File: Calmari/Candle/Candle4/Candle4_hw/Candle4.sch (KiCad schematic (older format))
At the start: 59 parts, among them Q1 LED_RGB, SW1 BUTTON, SW2 BUTTON, SW3 BUTTON

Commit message: 
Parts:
- removed RP1, RP2, RP3: REFPOINT, symbol REFPOINT
- R1: value 20k -> 30k
- R7, R8: value 10R -> 51R
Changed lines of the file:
@@
 EESchema Schematic File Version 2
-LIBS:Connectors_kl
-LIBS:pcb_details
-LIBS:RF ICs
-LIBS:st_kl
-LIBS:Tittar_kl
-LIBS:power
-LIBS:Antennas_kl
-LIBS:Power_kl
 LIBS:Candle4-cache
 EELAYER 27 0
@@
 NoConn ~ 5250 3000
 NoConn ~ 5250 2700
-NoConn ~ 5250 2600
 NoConn ~ 5250 2500
 NoConn ~ 5250 2400
@@
 P 12100 7150
 F 0 "R7" V 12180 7000 50  0000 C CNN
-F 1 "10R" V 12100 7150 50  0000 C CNN
+F 1 "51R" V 12100 7150 50  0000 C CNN
 F 2 "RES_0603" V 12180 7250 28  0000 C CNN
 F 3 "~" H 12100 7150 60  0000 C CNN
@@
 P 12100 7350
 F 0 "R8" V 12180 7200 50  0000 C CNN
-F 1 "10R" V 12100 7350 50  0000 C CNN
+F 1 "51R" V 12100 7350 50  0000 C CNN
 F 2 "RES_0603" V 12180 7450 28  0000 C CNN
 F 3 "~" H 12100 7350 60  0000 C CNN
@@
 $EndComp
 $Comp
-L REFPOINT RP1
-U 1 1 4DC45333
-P 15350 9550
-F 0 "RP1" H 15050 9550 60  0000 C CNN
-F 1 "REFPOINT" H 14700 9550 60  0000 C CNN
-F 2 "" H 15350 9550 60  0001 C CNN
-F 3 "" H 15350 9550 60  0001 C CNN
-	1    15350 9550
-	1    0    0    -1
-$EndComp
-$Comp
-L REFPOINT RP2
-U 1 1 4DC4533D
-P 15350 9800
-F 0 "RP2" H 15050 9800 60  0000 C CNN
-F 1 "REFPOINT" H 14700 9800 60  0000 C CNN
-F 2 "" H 15350 9800 60  0001 C CNN
-F 3 "" H 15350 9800 60  0001 C CNN
-	1    15350 9800
-	1    0    0    -1
-$EndComp
-$Comp
-L REFPOINT RP3
-U 1 1 51E196D1
-P 15350 10050
-F 0 "RP3" H 15050 10050 60  0000 C CNN
-F 1 "REFPOINT" H 14700 10050 60  0000 C CNN
-F 2 "" H 15350 10050 60  0001 C CNN
-F 3 "" H 15350 10050 60  0001 C CNN
-	1    15350 10050
-	1    0    0    -1
-$EndComp
-$Comp
 L CRYSTAL_H XTAL1
 U 1 1 51E1A3DF
@@
 	1    0    0    -1
 $EndComp
-Text Label 7900 3000 0    60   ~ 0
+Text Label 4850 2200 0    60   ~ 0
 LED_R
-Text Label 7900 3200 0    60   ~ 0
+Text Label 4850 2300 0    60   ~ 0
 LED_G
-Text Label 7900 3300 0    60   ~ 0
+Text Label 4850 2600 0    60   ~ 0
 LED_B
-NoConn ~ 5250 2300
 NoConn ~ 5250 3500
 NoConn ~ 5250 3600
@@
 P 1500 7900
 F 0 "R1" V 1580 7750 50  0000 C CNN
-F 1 "20k" V 1500 7900 50  0000 C CNN
+F 1 "30k" V 1500 7900 50  0000 C CNN
 F 2 "RES_0603" V 1580 8000 28  0000 C CNN
 F 3 "~" H 1500 7900 60  0000 C CNN
@@
 Wire Wire Line
 	1650 5800 1500 5800
-Connection ~ 1500 5800
 Wire Wire Line
 	1500 6400 1650 6400
@@
 	9750 4550 9850 4550
 Wire Wire Line
-	7900 3000 7750 3000
-Wire Wire Line
-	7750 3200 7900 3200
-Wire Wire Line
-	7900 3300 7750 3300
-Wire Wire Line
 	5250 3900 5100 3900
 Wire Wire Line
@@
 Wire Wire Line
 	1500 5800 1500 7650
-NoConn ~ 5250 2200
 Text Notes 4550 8300 0    60   ~ 0
 +BATTERY
 Text Notes 4550 8800 0    60   ~ 0
 -BATTERY
+NoConn ~ 7750 3000
+NoConn ~ 7750 3200
+NoConn ~ 7750 3300
+Wire Wire Line
+	4850 2200 5250 2200
+Wire Wire Line
+	5250 2300 4850 2300
+Wire Wire Line
+	4850 2600 5250 2600
 $EndSCHEMATC

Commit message: Candle4 pcb added
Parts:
- C6, C7, C8, C9: footprint CAP_0603 -> CAP_0402
- R1, R2, R3, R4, R6, R7, R8: footprint RES_0603 -> RES_0402
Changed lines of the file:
@@
 EESchema Schematic File Version 2
+LIBS:Connectors_kl
+LIBS:pcb_details
+LIBS:RF ICs
+LIBS:st_kl
+LIBS:Tittar_kl
+LIBS:power
+LIBS:Antennas_kl
+LIBS:Power_kl
 LIBS:Candle4-cache
 EELAYER 27 0
@@
 Sheet 1 1
 Title ""
-Date "22 feb 2015"
+Date "3 mar 2015"
 Rev ""
 Comp ""
@@
 F 0 "R7" V 12180 7000 50  0000 C CNN
 F 1 "51R" V 12100 7150 50  0000 C CNN
-F 2 "RES_0603" V 12180 7250 28  0000 C CNN
+F 2 "RES_0402" V 12180 7250 28  0000 C CNN
 F 3 "~" H 12100 7150 60  0000 C CNN
 	1    12100 7150
@@
 F 0 "R8" V 12180 7200 50  0000 C CNN
 F 1 "51R" V 12100 7350 50  0000 C CNN
-F 2 "RES_0603" V 12180 7450 28  0000 C CNN
+F 2 "RES_0402" V 12180 7450 28  0000 C CNN
 F 3 "~" H 12100 7350 60  0000 C CNN
 	1    12100 7350
@@
 F 0 "R6" V 12180 6800 50  0000 C CNN
 F 1 "51R" V 12100 6950 50  0000 C CNN
-F 2 "RES_0603" V 12180 7050 28  0000 C CNN
+F 2 "RES_0402" V 12180 7050 28  0000 C CNN
 F 3 "~" H 12100 6950 60  0000 C CNN
 	1    12100 6950
@@
 F 0 "C7" H 6450 8450 50  0000 L CNN
 F 1 "10u" H 6600 8650 50  0000 L CNN
-F 2 "CAP_0603" V 6650 8400 28  0000 C BNN
+F 2 "CAP_0402" V 6650 8400 28  0000 C BNN
 F 3 "~" H 6550 8550 60  0000 C CNN
 	1    6550 8550
@@
 F 0 "C6" H 6050 8450 50  0000 L CNN
 F 1 "0.1u" H 5950 8650 50  0000 L CNN
-F 2 "CAP_0603" V 6250 8400 28  0000 C BNN
+F 2 "CAP_0402" V 6250 8400 28  0000 C BNN
 F 3 "~" H 6150 8550 60  0000 C CNN
 	1    6150 8550
@@
 F 0 "C8" H 8700 8450 50  0000 L CNN
 F 1 "0.1u" H 8600 8650 50  0000 L CNN
-F 2 "CAP_0603" V 8900 8400 28  0000 C BNN
+F 2 "CAP_0402" V 8900 8400 28  0000 C BNN
 F 3 "~" H 8800 8550 60  0000 C CNN
 	1    8800 8550
@@
 F 0 "C9" H 9100 8450 50  0000 L CNN
 F 1 "10u" H 9250 8650 50  0000 L CNN
-F 2 "CAP_0603" V 9300 8400 28  0000 C BNN
+F 2 "CAP_0402" V 9300 8400 28  0000 C BNN
 F 3 "~" H 9200 8550 60  0000 C CNN
 	1    9200 8550
@@
 F 0 "R1" V 1580 7750 50  0000 C CNN
 F 1 "30k" V 1500 7900 50  0000 C CNN
-F 2 "RES_0603" V 1580 8000 28  0000 C CNN
+F 2 "RES_0402" V 1580 8000 28  0000 C CNN
 F 3 "~" H 1500 7900 60  0000 C CNN
 	1    1500 7900
@@
 F 0 "R2" V 2980 5650 50  0000 C CNN
 F 1 "4k7" V 2900 5800 50  0000 C CNN
-F 2 "RES_0603" V 2980 5900 28  0000 C CNN
+F 2 "RES_0402" V 2980 5900 28  0000 C CNN
 F 3 "~" H 2900 5800 60  0000 C CNN
 	1    2900 5800
@@
 F 0 "R3" V 2980 6250 50  0000 C CNN
 F 1 "4k7" V 2900 6400 50  0000 C CNN
-F 2 "RES_0603" V 2980 6500 28  0000 C CNN
+F 2 "RES_0402" V 2980 6500 28  0000 C CNN
 F 3 "~" H 2900 6400 60  0000 C CNN
 	1    2900 6400
@@
 F 0 "R4" V 2980 6850 50  0000 C CNN
 F 1 "4k7" V 2900 7000 50  0000 C CNN
-F 2 "RES_0603" V 2980 7100 28  0000 C CNN
+F 2 "RES_0402" V 2980 7100 28  0000 C CNN
 F 3 "~" H 2900 7000 60  0000 C CNN
 	1    2900 7000

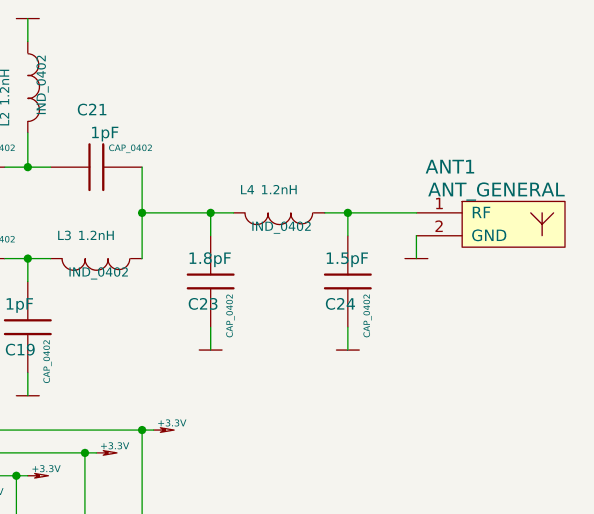
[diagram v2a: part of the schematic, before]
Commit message: 
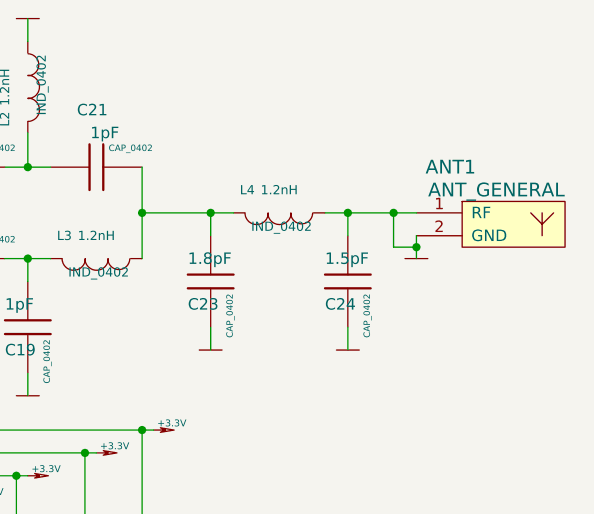
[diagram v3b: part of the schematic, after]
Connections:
- wire segments 172 -> 174
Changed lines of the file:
@@
 Sheet 1 1
 Title ""
-Date "3 mar 2015"
+Date "5 mar 2015"
 Rev ""
 Comp ""
@@
 Wire Wire Line
 	4850 2600 5250 2600
+Wire Wire Line
+	14700 2900 14600 2900
+Wire Wire Line
+	14600 2900 14600 2750
+Connection ~ 14600 2750
+Connection ~ 14700 2900
 $EndSCHEMATC

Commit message: gerber added
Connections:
- wire segments 174 -> 172
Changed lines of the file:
@@
 Sheet 1 1
 Title ""
-Date "5 mar 2015"
+Date "28 mar 2015"
 Rev ""
 Comp ""
@@
 Wire Wire Line
 	4850 2600 5250 2600
-Wire Wire Line
-	14700 2900 14600 2900
-Wire Wire Line
-	14600 2900 14600 2750
-Connection ~ 14600 2750
-Connection ~ 14700 2900
 $EndSCHEMATC
